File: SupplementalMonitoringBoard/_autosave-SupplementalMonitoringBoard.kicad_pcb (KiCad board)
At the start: 2 copper layers, 129 x 134 mm, 44 parts, among them J1 PeripheralCANConnector, U1 OPA842xDBV, U2 OPA842xDBV, U3 INA180B1, U4 PAMC131M03QDFMRQ1, U5 PeripheralSOM

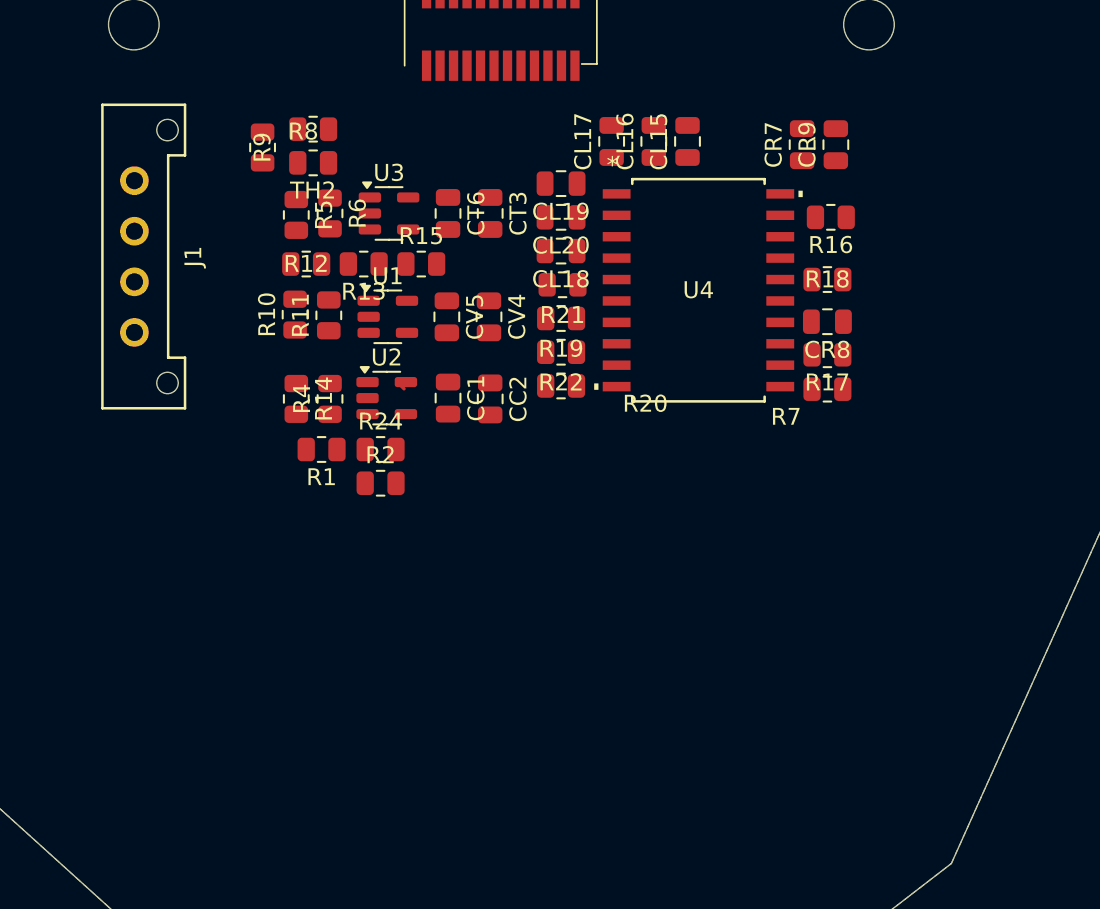
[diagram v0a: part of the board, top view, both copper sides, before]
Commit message: Adressed Reviews - Supplemental Monitoring Board
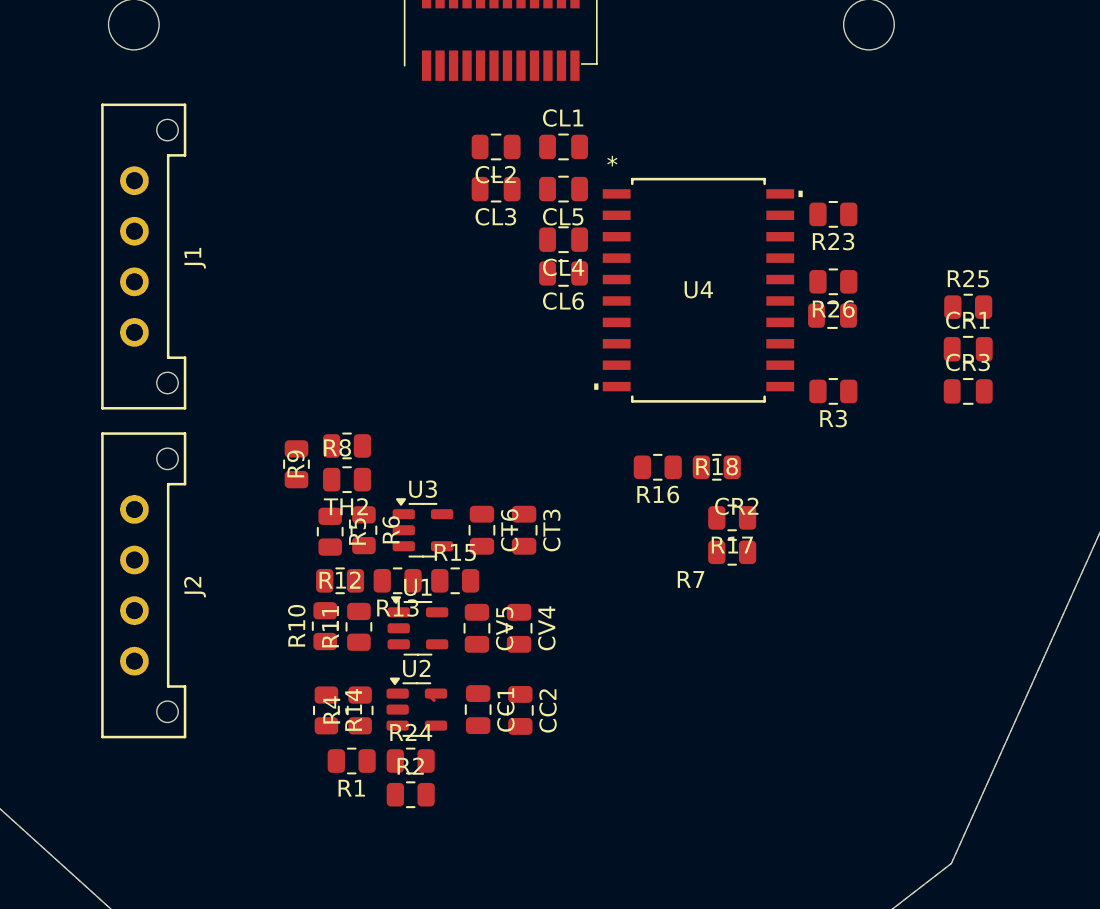
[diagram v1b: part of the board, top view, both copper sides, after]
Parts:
- removed CL15, CL18, CR8: 100nF, Capacitor_SMD:C_0805_2012Metric
- removed CL16, CL19, CL20, CR7: 1nF, Capacitor_SMD:C_0805_2012Metric
- removed CL17, CR9: 1uF, Capacitor_SMD:C_0805_2012Metric
- removed R19, R20: 2.6k, Resistor_SMD:R_0805_2012Metric
- removed R21, R22: 10k, Resistor_SMD:R_0805_2012Metric
- added CL1: 100nF, Capacitor_SMD:C_0805_2012Metric, F.Cu at (135.0, 103.0)
- added CL2: 1nF, Capacitor_SMD:C_0805_2012Metric, F.Cu at (131.0, 103.0)
- added CL3: 1uF, Capacitor_SMD:C_0805_2012Metric, F.Cu at (131.0, 105.5)
- added CL4: 100nF, Capacitor_SMD:C_0805_2012Metric, F.Cu at (135.0, 108.5)
- added CL5: 1nF, Capacitor_SMD:C_0805_2012Metric, F.Cu at (135.0, 105.5)
- added CL6: 1nF, Capacitor_SMD:C_0805_2012Metric, F.Cu at (135.0, 110.5)
- added CR1: 1nF, Capacitor_SMD:C_0805_2012Metric, F.Cu at (159.0, 115.0)
- added CR2: 100nF, Capacitor_SMD:C_0805_2012Metric, F.Cu at (150.9, 113.0)
- added CR3: 1uF, Capacitor_SMD:C_0805_2012Metric, F.Cu at (159.0, 117.5)
- added J2: PeripheralCANConnector, UTSVT_Connectors:Molex_MicroFit3.0_1x4xP3.00mm_PolarizingPeg_Vertical, F.Cu at (109.5, 124.5)
- added R23: 100k, Resistor_SMD:R_0805_2012Metric, F.Cu at (151.0, 107.0)
- added R25: 100k, Resistor_SMD:R_0805_2012Metric, F.Cu at (159.0, 112.5)
- added R26: 100k, Resistor_SMD:R_0805_2012Metric, F.Cu at (151.0, 111.0)
- added R3: 100k, Resistor_SMD:R_0805_2012Metric, F.Cu at (151.0, 117.5)
- R10, R5: value 30k -> 40k
- R14: value 10 -> 150K
- R15: value 5k -> 3k
- R16: value 100k -> 30k
- R17, R18: value 100k -> 10k
- R2: value 30k -> 50K
- R4: value 10k -> 10K
- R7: value 100k -> 30K
- moved CT3 18.9 mm to (132.7, 125.7)
- moved CT6 18.9 mm to (130.2, 125.7)
- moved R6 18.9 mm to (123.2, 125.7)
- moved R8 18.9 mm to (122.2, 120.7)
- moved TH2 18.9 mm to (122.2, 122.7)
- moved U3 18.9 mm to (126.7, 125.7)
- moved R12 18.9 mm to (121.7, 128.7)
- moved R15 18.9 mm to (128.6, 128.7)
- moved R13 18.9 mm to (125.2, 128.7)
- moved R5 18.9 mm to (121.2, 125.8)
- moved R9 18.9 mm to (119.2, 121.8)
- moved CC1 18.6 mm to (129.9, 136.4)
- moved CV4 18.6 mm to (132.4, 131.6)
- moved CV5 18.6 mm to (129.9, 131.6)
- moved R11 18.6 mm to (122.9, 131.5)
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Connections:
- net /ADC Connect/DCDC_OUT renamed /DCDC_OUT
- R16 pad 1: /LowPower -> /AINOP
- R16 pad 2: /*CS -> +BATT
- R17 pad 1: /LowPower -> /AIN12N
- R17 pad 2: /DOUT -> GND
- R18 pad 1: /LowPower -> /AINOP
- R18 pad 2: /*DRDY -> GND
- R7 pad 1: /LowPower -> /AIN12N
- R7 pad 2: /*SYNC/*RESET -> +BATT
- U4 pad 13: /ADC Output/DVDD -> /DVDD
- U4 pad 14: GND -> /DCDC_CAP
- U4 pad 15: /LowPower -> GND
- U4 pad 4: /ADC Connect/HLDO_OUT -> /HLDO_OUT
- U4 pad 7: /GNDVoltage/AIN12N -> /AIN12N
- U4 pad 9: /GNDVoltage/AIN0P -> /AINOP
- U5 pad 10: /LowPower -> /DVDD

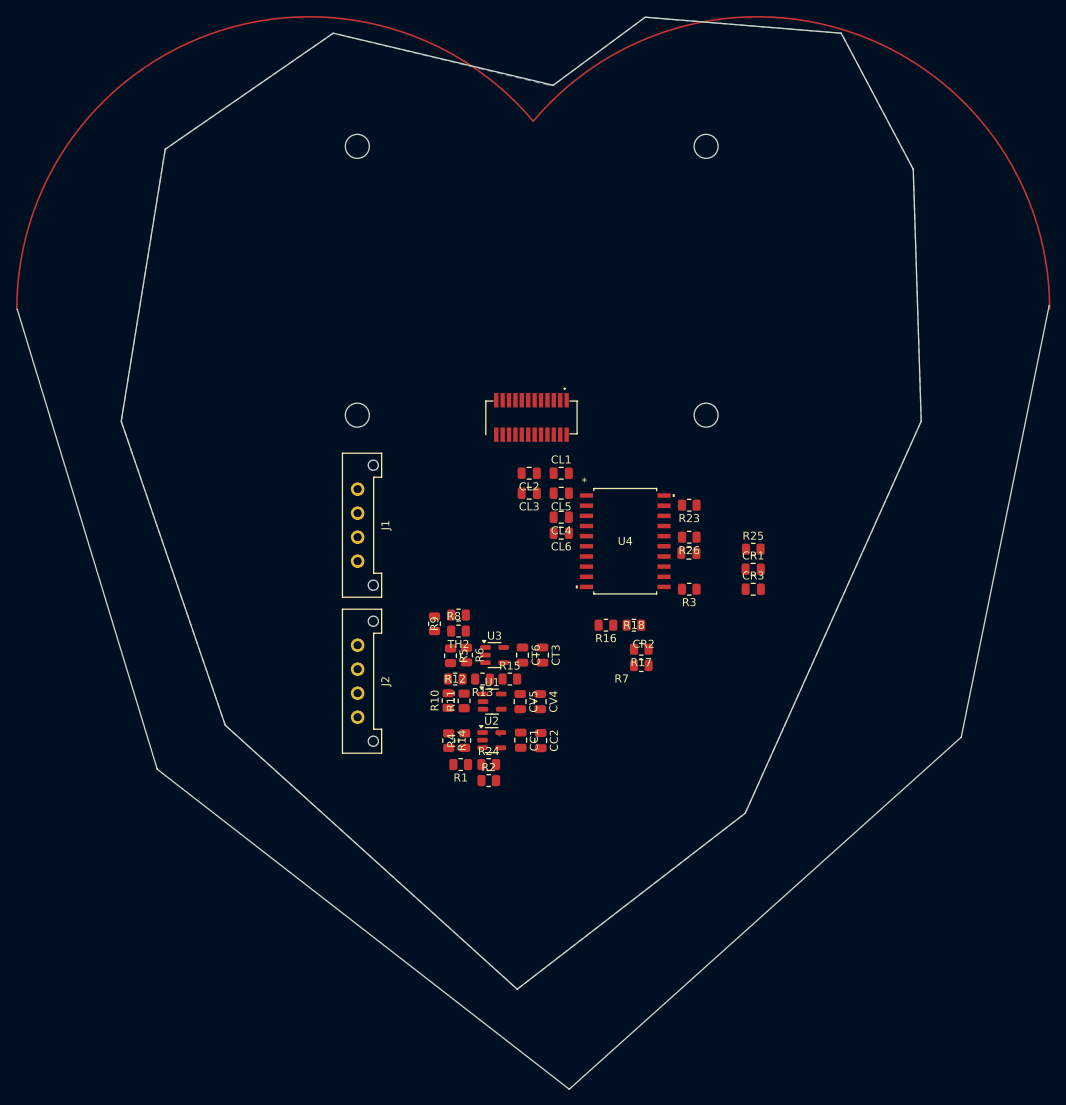
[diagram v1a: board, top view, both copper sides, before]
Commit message: PCB Layout - Supplemental Monitoring Board
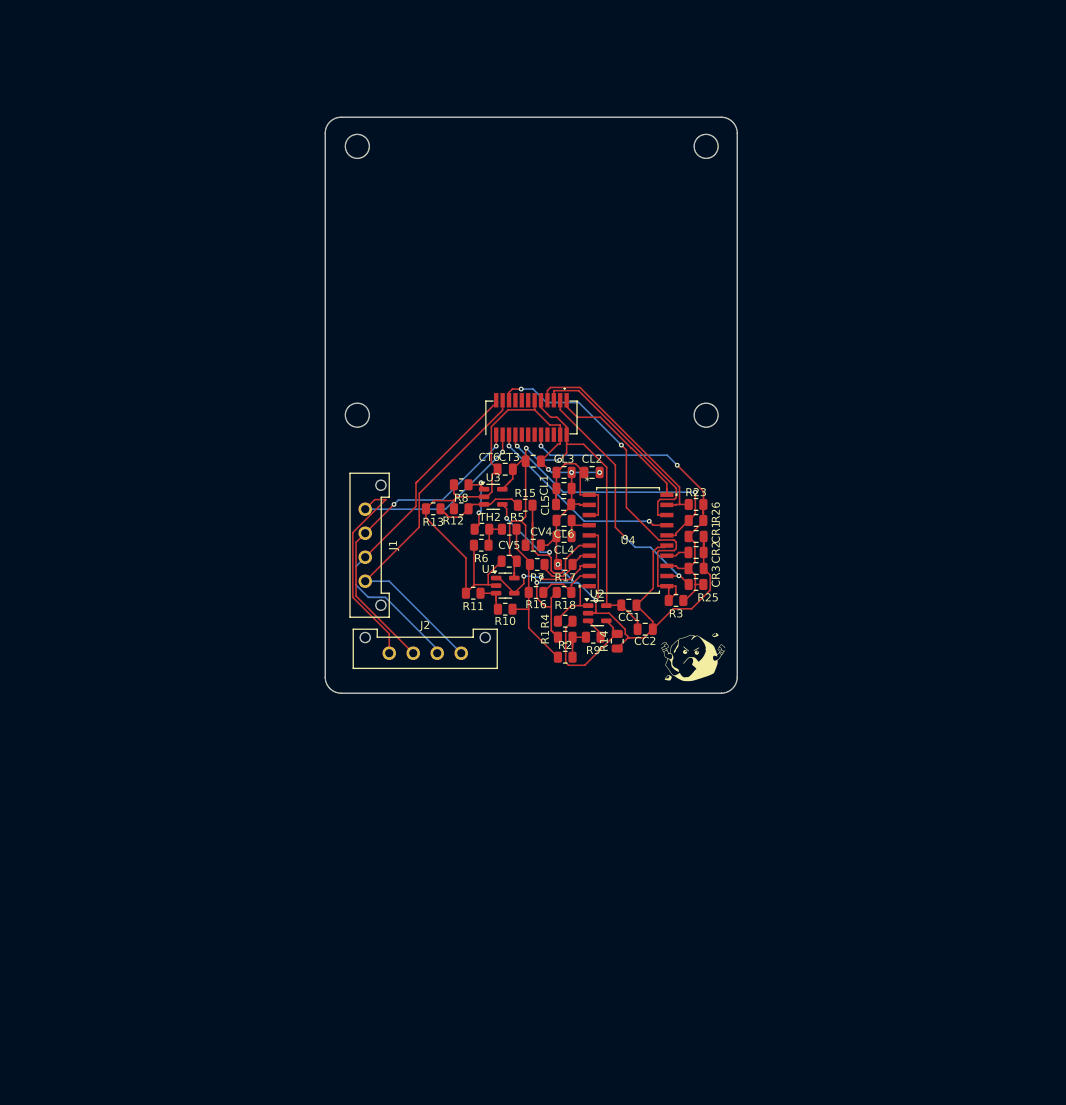
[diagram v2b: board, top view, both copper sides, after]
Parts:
- removed R24: .33, Resistor_SMD:R_0805_2012Metric
- added G***: LOGO, LOGO, F.Cu at (151.5, 126.0)
- R8, TH2: value 1k -> 500
- R9: value 1k -> .01
- moved R14 24.5 mm to (142.0, 124.0), turned to 90 degrees
- moved CT3 24.3 mm to (131.5, 101.5), turned to 0 degrees
- moved CT6 23.3 mm to (128.0, 102.5), turned to 180 degrees
- moved R13 22.2 mm to (119.0, 107.5)
- moved R15 21.8 mm to (130.5, 107.0)
- moved CC1 21.6 mm to (143.4, 119.5), turned to 0 degrees
- moved R12 21.3 mm to (122.5, 107.5), turned to 0 degrees
- moved U2 20.6 mm to (139.5, 120.5)
- moved R1 20.6 mm to (135.5, 123.5)
- moved R9 19.9 mm to (139.0, 123.5), turned to 180 degrees
- moved U3 19.8 mm to (126.5, 106.0)
- moved CV4 19.6 mm to (131.5, 112.0), turned to 0 degrees
- moved R4 19.5 mm to (135.5, 121.5), turned to 180 degrees
- moved CC2 19.1 mm to (145.5, 122.5), turned to 0 degrees
- moved R2 18.1 mm to (135.5, 126.0), turned to 180 degrees
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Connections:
- R1 pad 1: Net-(U2-+) -> Net-(R1-Pad1)
- R2 pad 1: Net-(U2-+) -> Net-(R1-Pad1)
- R9 pad 1: /Temperature/Thermistor -> Net-(U2-+)
- R9 pad 2: Net-(U3-+) -> Net-(R1-Pad1)
- U3 pad 1: Net-(U3-+) -> /Temperature/Thermistor
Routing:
- net GND: track 0.00 -> 167.1 mm, vias 0 -> 6
- net +3.3V: track 0.44 -> 71.0 mm, vias 0 -> 2
- net +12V: track 0.00 -> 48.2 mm, vias 0 -> 1
- net /*SYNC/*RESET: track 0.00 -> 47.5 mm, vias 0 -> 2
- net /DVDD: track 0.00 -> 45.7 mm, vias 0 -> 2
- net /CAN_L: track 0.00 -> 45.5 mm
- net /CAN_H: track 0.00 -> 44.6 mm
- net GNDPWR: track 0.00 -> 40.8 mm, vias 0 -> 2
- net /*DRDY: track 0.00 -> 33.7 mm, vias 0 -> 2
- net /DOUT: track 0.00 -> 32.4 mm, vias 0 -> 2
- net /AIN2P/GPO: track 0.00 -> 29.7 mm, vias 0 -> 2
- net /SCLK: track 0.00 -> 28.0 mm
- net /*CS: track 0.00 -> 28.0 mm
- net /CLKIN: track 0.00 -> 25.2 mm, vias 0 -> 2
- net +BATT: track 0.00 -> 20.8 mm
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- removed copper zone on B.Cu, net GND
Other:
- board size 129 x 134 mm -> 51.5 x 72 mm

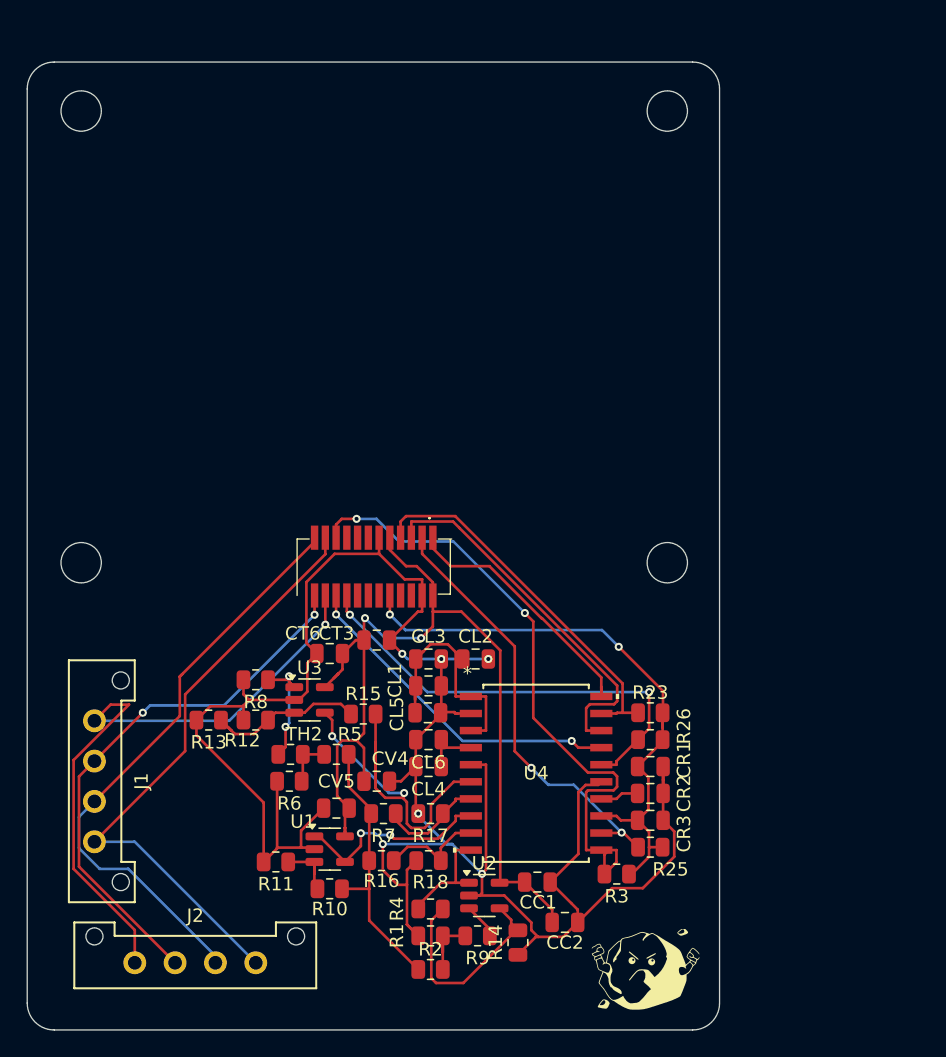
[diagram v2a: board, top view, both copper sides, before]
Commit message: Supplemental Monitoring Board - Layout
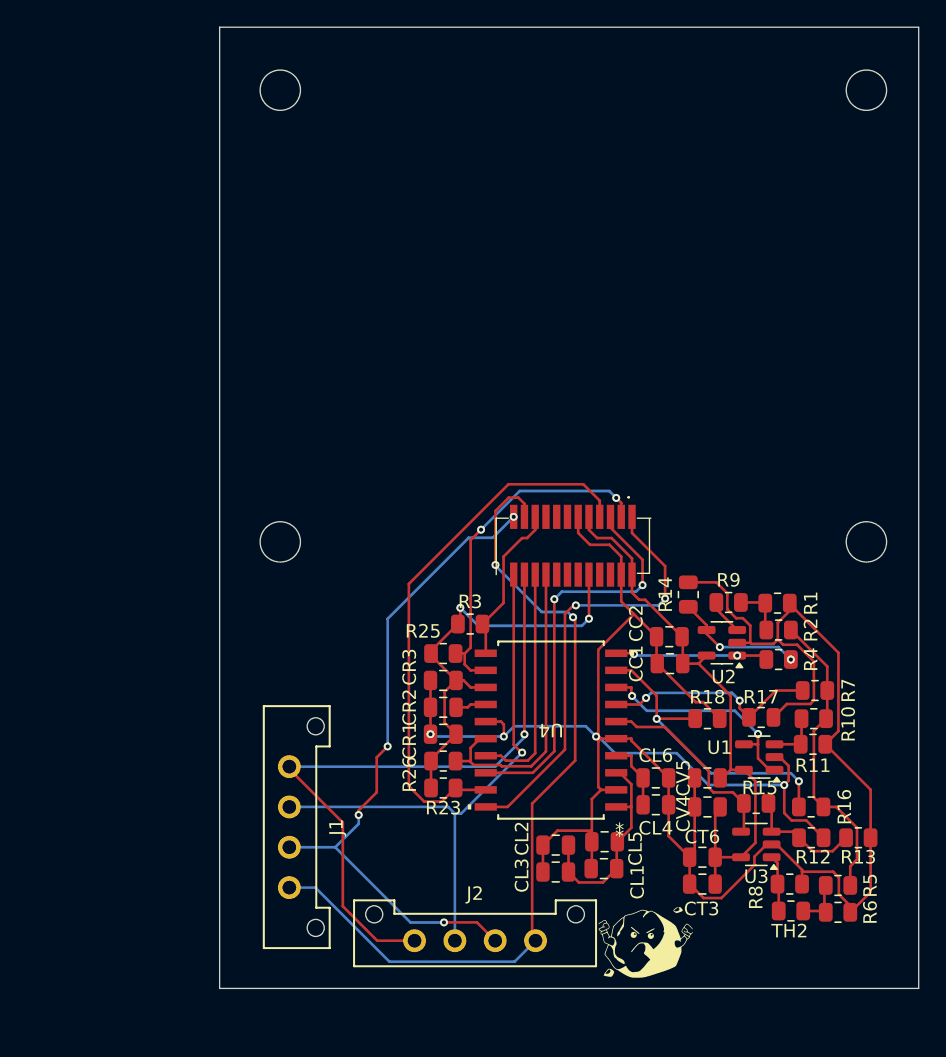
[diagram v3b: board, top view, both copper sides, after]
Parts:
- moved R13 49.1 mm to (167.3, 116.2), turned to 0 degrees
- moved R8 42.5 mm to (162.2, 119.7), turned to 0 degrees
- moved R12 42.2 mm to (163.8, 116.2), turned to 180 degrees
- moved R6 42.0 mm to (165.8, 121.8), turned to 0 degrees
- moved R11 40.9 mm to (163.9, 109.2), turned to 0 degrees
- moved TH2 39.0 mm to (162.3, 121.7)
- moved R5 38.6 mm to (165.8, 119.8)
- moved R10 38.2 mm to (164.0, 107.3)
- moved R2 36.2 mm to (161.4, 100.8), turned to 0 degrees
- moved R1 35.8 mm to (161.3, 98.8), turned to 0 degrees
- moved U3 34.9 mm to (159.7, 116.7), turned to 180 degrees
- moved R7 33.4 mm to (164.1, 105.2), turned to 0 degrees
- moved U1 32.7 mm to (159.9, 110.2), turned to 180 degrees
- moved R16 32.2 mm to (163.8, 113.9), turned to 0 degrees
- moved R4 31.9 mm to (161.4, 102.9)
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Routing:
- net /*SYNC/*RESET: track 47.5 -> 12.1 mm, vias 2 -> 0
- net +3.3V: track 71.0 -> 42.7 mm, vias 2 -> 0
- net /CAN_L: track 45.5 -> 62.1 mm, vias 0 -> 2
- net GND: track 167.1 -> 182.2 mm, vias 6 -> 4
- net /AINOP: track 7.99 -> 22.8 mm, vias 0 -> 2
- net /AIN2P/GPO: track 29.7 -> 14.9 mm, vias 2 -> 0
- net /DIN: track 19.4 -> 32.8 mm, vias 0 -> 2
- net /DVDD: track 45.7 -> 32.6 mm
- net /*CS: track 28.0 -> 40.7 mm
- net /*DRDY: track 33.7 -> 22.9 mm, vias 2 -> 0
- net /AIN12N: track 8.24 -> 16.1 mm, vias 0 -> 2
- net /CLKIN: track 25.2 -> 17.3 mm, vias 2 -> 0
- net /DOUT: track 32.4 -> 26.0 mm
- net Net-(U2--): track 16.0 -> 9.63 mm, vias 0 -> 2
- net /CAN_H: track 44.6 -> 49.5 mm, vias 0 -> 4
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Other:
- board size 51.5 x 72 mm -> 52 x 71.5 mm
